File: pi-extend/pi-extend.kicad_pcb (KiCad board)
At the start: 2 copper layers, 53.3 x 67.1 mm, 5 parts, among them J1 Conn_02x20_Odd_Even, J2 Conn_01x20_Male, J3 Conn_01x20_Male, J4 Conn_01x02_Male, J5 Conn_01x02_Male

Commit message: pi extender 레이아웃 축소
Signed-off-by: Ju, Gyeong-min <jcmh74@gmail.com>
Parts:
- moved J4 21.4 mm to (138.7, 111.8)
- moved J5 21.4 mm to (186.9, 111.8)
- moved J2 12.2 mm to (148.8, 78.8)
- moved J3 12.2 mm to (176.8, 78.8)
- moved J1 12.1 mm to (138.7, 67.6)
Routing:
- net Net-(J1-Pad2): track 102.9 -> 86.5 mm
- net Net-(J1-Pad1): track 73.1 -> 57.1 mm
- net Net-(J1-Pad5): track 73.5 -> 57.5 mm
- net Net-(J1-Pad10): track 93.7 -> 78.0 mm
- net Net-(J1-Pad29): track 76.8 -> 76.0 mm
- net Net-(J1-Pad7): track 32.0 -> 31.2 mm
- net Net-(J1-Pad40): track 68.0 -> 67.2 mm
- net Net-(J1-Pad3): track 26.6 -> 25.8 mm
- net Net-(J1-Pad38): track 66.1 -> 65.4 mm
- net Net-(J1-Pad34): track 62.4 -> 61.6 mm
- net Net-(J1-Pad36): track 64.3 -> 63.5 mm
- net Net-(J1-Pad18): track 55.5 -> 56.1 mm
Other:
- board size 53.3 x 67.1 mm -> 53.4 x 65.9 mm
- board text added: "3V3 G2(SDA1) G3(SCL1) G4 GND G17 G27 G22 3V3 G10(MOSI) G9(MISO) G11(SCLK) GND ID_SD G5 G6 G13 G19 G26 GND"
- board text added: "5V 5V GND G14(TXD0) G15(RXD0) G18 GND G23 G24 GND G25 G8(CE0) G7(CE1) ID_SC GND G12 GND G16 G20 G21"
- board text removed: "3V3 SDA1 SCL1 GP4 GND GP17 GP27 GP22 3V3 MOSI MISO SCLK GND EED GP5 GP6 GP13 GP19 GP26 GND"
- board text removed: "5V 5V GND TXD0 RXD0 GP18 GND GP23 GP24 GND GP25 CE0 CE1 EEC GND GP12 GND GP16 GP20 GP21"

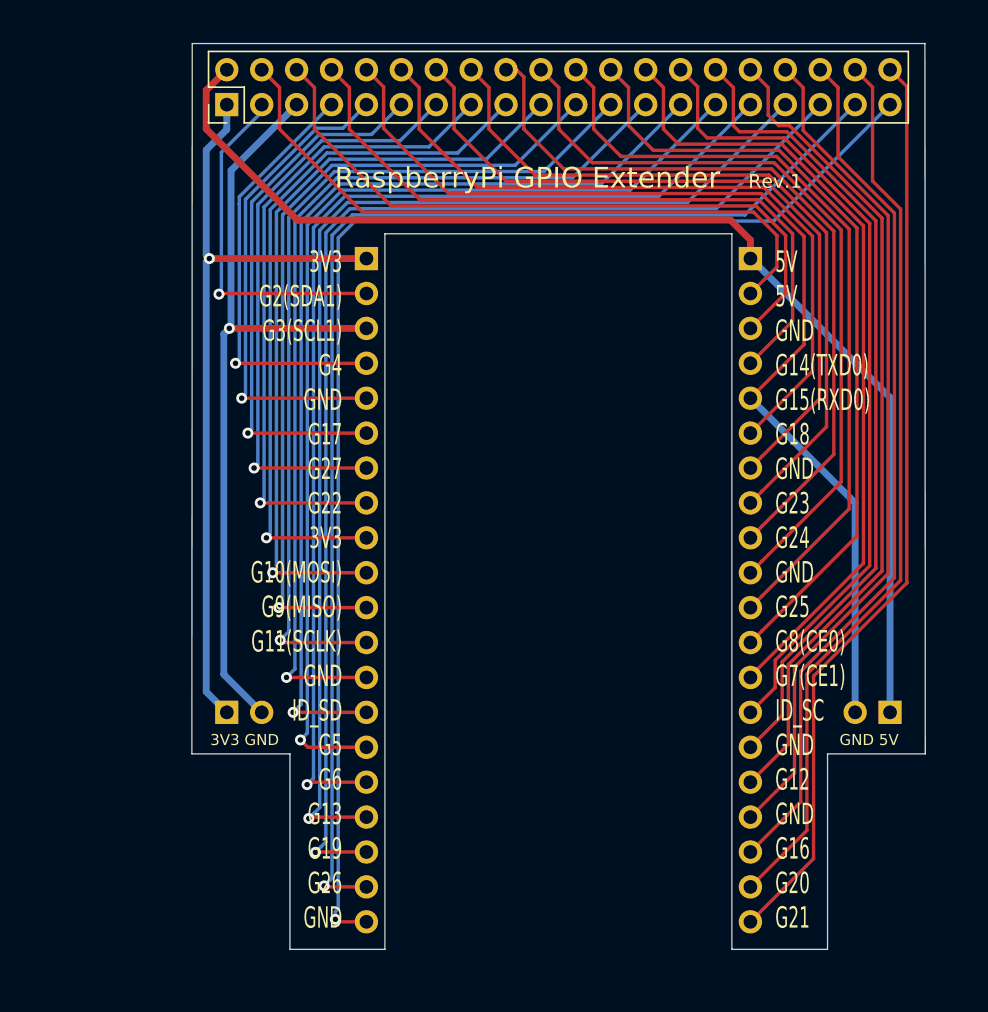
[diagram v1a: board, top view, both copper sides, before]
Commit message: pi-extender 레이아웃 변경
Signed-off-by: Ju, Gyeong-min <jcmh74@gmail.com>
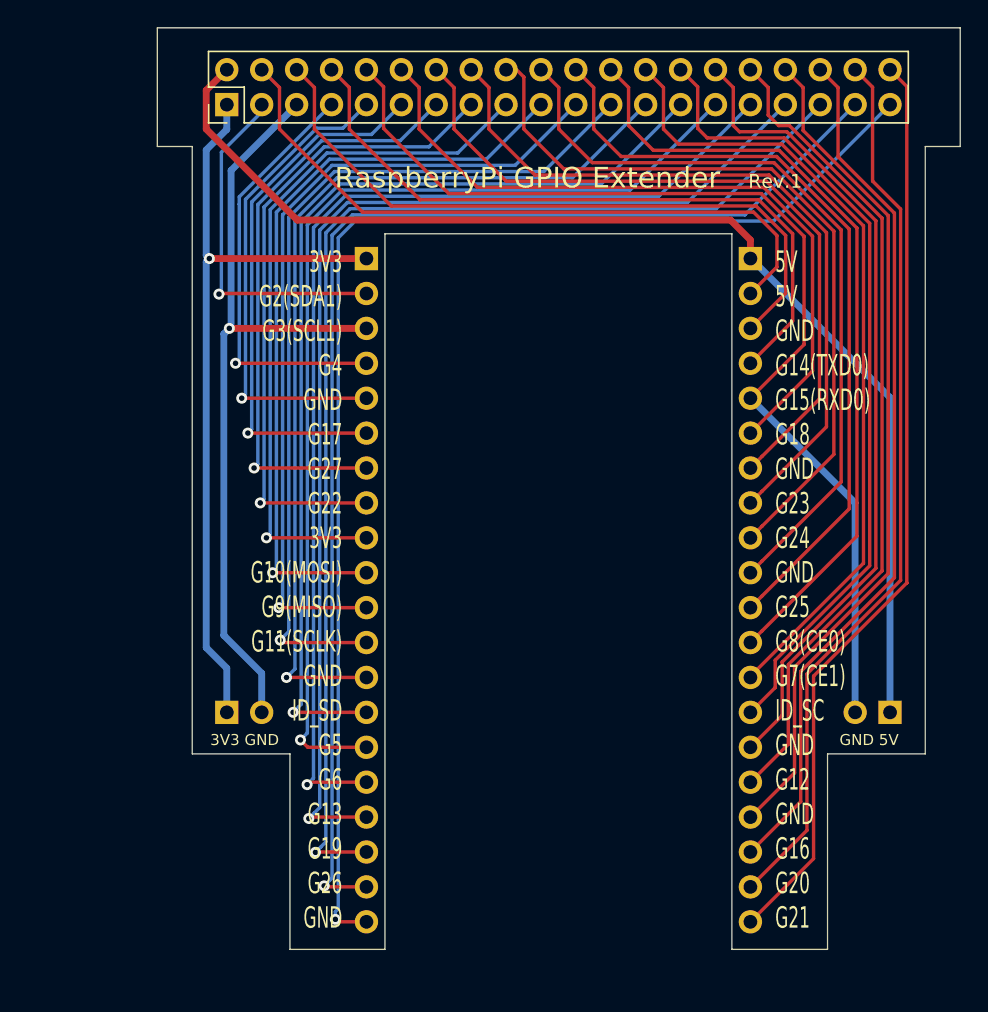
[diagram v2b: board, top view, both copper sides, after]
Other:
- board size 53.4 x 65.9 mm -> 58.4 x 67.1 mm
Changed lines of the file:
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@@
   (general
     (thickness 1.6)
-    (drawings 18)
-    (tracks 318)
+    (drawings 22)
+    (tracks 320)
     (zones 0)
     (modules 5)
@@
     )
   )
+  (gr_line (start 189.484 70.612) (end 189.484 114.808) (layer Edge.Cuts) (width 0.05))
+  (gr_line (start 189.484 70.612) (end 192.024 70.612) (layer Edge.Cuts) (width 0.05))
+  (gr_line (start 136.144 70.612) (end 136.144 114.808) (layer Edge.Cuts) (width 0.05))
+  (gr_line (start 136.144 70.612) (end 133.604 70.612) (layer Edge.Cuts) (width 0.05))
   (gr_line (start 143.256 114.808) (end 143.256 129.032) (layer Edge.Cuts) (width 0.05))
-  (gr_line (start 143.256 114.808) (end 136.1186 114.808) (layer Edge.Cuts) (width 0.05))
+  (gr_line (start 143.256 114.808) (end 136.144 114.808) (layer Edge.Cuts) (width 0.05))
   (gr_line (start 182.372 114.808) (end 182.372 129.032) (layer Edge.Cuts) (width 0.05))
   (gr_line (start 189.484 114.808) (end 182.372 114.808) (layer Edge.Cuts) (width 0.05))
@@
   (gr_line (start 150.1648 129.032) (end 150.1648 76.962) (layer Edge.Cuts) (width 0.05))
   (gr_line (start 143.256 129.032) (end 150.1648 129.032) (layer Edge.Cuts) (width 0.05))
-  (gr_line (start 136.144 63.119) (end 136.1186 114.808) (layer Edge.Cuts) (width 0.05))
-  (gr_line (start 189.4586 63.119) (end 136.144 63.119) (layer Edge.Cuts) (width 0.05))
-  (gr_line (start 189.484 114.808) (end 189.4586 63.119) (layer Edge.Cuts) (width 0.05))
+  (gr_line (start 133.604 61.976) (end 133.604 70.612) (layer Edge.Cuts) (width 0.05))
+  (gr_line (start 192.024 61.976) (end 133.604 61.976) (layer Edge.Cuts) (width 0.05))
+  (gr_line (start 192.024 70.612) (end 192.024 61.976) (layer Edge.Cuts) (width 0.05))
   (gr_line (start 175.4124 129.032) (end 182.372 129.032) (layer Edge.Cuts) (width 0.05))
   (gr_line (start 175.4124 76.962) (end 175.4124 129.032) (layer Edge.Cuts) (width 0.05))
@@
   (segment (start 138.6586 67.564) (end 138.6586 69.3674) (width 0.5) (layer B.Cu) (net 1))
   (segment (start 137.16 78.994) (end 137.3886 78.7654) (width 0.5) (layer B.Cu) (net 1))
-  (segment (start 137.16 110.2868) (end 137.16 78.994) (width 0.5) (layer B.Cu) (net 1))
-  (segment (start 138.6586 111.7854) (end 137.16 110.2868) (width 0.5) (layer B.Cu) (net 1))
+  (segment (start 137.16 107.0737) (end 137.16 78.994) (width 0.5) (layer B.Cu) (net 1))
+  (segment (start 138.6586 108.5723) (end 137.16 107.0737) (width 0.5) (layer B.Cu) (net 1))
+  (segment (start 138.6586 111.7854) (end 138.6586 108.5723) (width 0.5) (layer B.Cu) (net 1))
   (segment (start 176.7586 77.4154) (end 176.7586 78.7654) (width 0.5) (layer F.Cu) (net 2))
   (segment (start 137.16 66.5226) (end 137.16 69.342) (width 0.5) (layer F.Cu) (net 2))
@@
   (segment (start 143.7386 67.564) (end 143.7386 67.5894) (width 0.5) (layer B.Cu) (net 5))
   (segment (start 138.443413 84.245397) (end 138.843412 83.845398) (width 0.5) (layer B.Cu) (net 5))
-  (segment (start 138.443413 109.030213) (end 138.443413 84.245397) (width 0.5) (layer B.Cu) (net 5))
-  (segment (start 141.1986 111.7854) (end 138.443413 109.030213) (width 0.5) (layer B.Cu) (net 5))
+  (segment (start 138.443413 106.185413) (end 138.443413 84.245397) (width 0.5) (layer B.Cu) (net 5))
+  (segment (start 141.1986 108.9406) (end 138.443413 106.185413) (width 0.5) (layer B.Cu) (net 5))
+  (segment (start 141.1986 111.7854) (end 141.1986 108.9406) (width 0.5) (layer B.Cu) (net 5))
   (segment (start 179.324 81.28) (end 179.324 77.087589) (width 0.25) (layer F.Cu) (net 6))
   (segment (start 176.7586 83.8454) (end 179.324 81.28) (width 0.25) (layer F.Cu) (net 6))

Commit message: pi-extender gnd 핀 위치 변경
Signed-off-by: Ju, Gyeong-min <jcmh74@gmail.com>
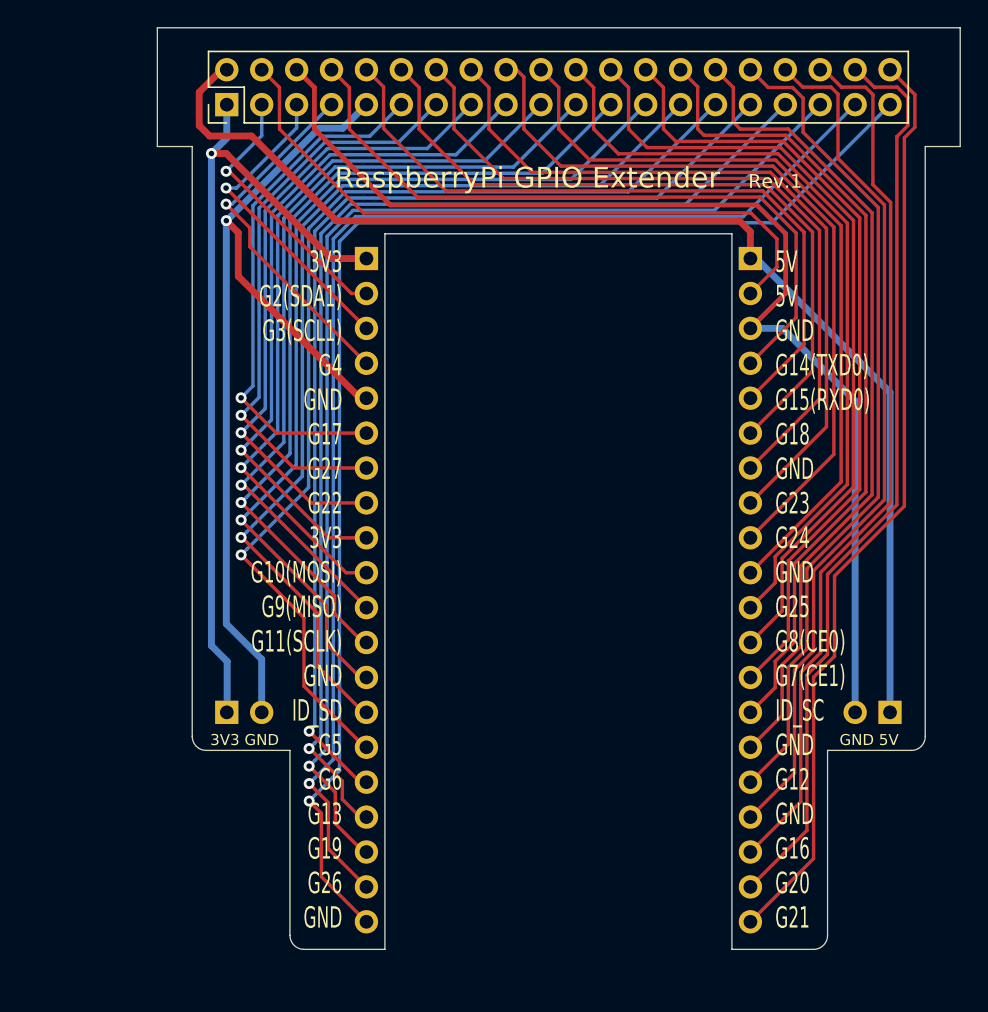
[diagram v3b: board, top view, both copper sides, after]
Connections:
- J4 pad 2: Net-(J1-Pad5) -> Net-(J1-Pad9)
- J5 pad 2: Net-(J1-Pad10) -> Net-(J1-Pad6)
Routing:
- net Net-(J1-Pad5): track 57.5 -> 23.1 mm
- net Net-(J1-Pad9): track 35.3 -> 67.9 mm
- net Net-(J1-Pad6): track 50.2 -> 82.7 mm
- net Net-(J1-Pad10): track 78.0 -> 52.2 mm
- net Net-(J1-Pad3): track 25.8 -> 19.8 mm
- net Net-(J1-Pad7): track 31.2 -> 26.5 mm
- net Net-(J1-Pad31): track 80.6 -> 77.8 mm
- net Net-(J1-Pad33): track 85.0 -> 82.5 mm
- net Net-(J1-Pad1): track 57.1 -> 59.6 mm
- net Net-(J1-Pad35): track 89.0 -> 87.0 mm
- net Net-(J1-Pad21): track 59.7 -> 58.2 mm
- net Net-(J1-Pad38): track 65.4 -> 66.9 mm
- net Net-(J1-Pad19): track 55.7 -> 54.2 mm
- net Net-(J1-Pad2): track 86.5 -> 87.9 mm
- net Net-(J1-Pad17): track 51.6 -> 50.3 mm
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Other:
- outline, holes or cut-outs redrawn

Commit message: pi-extend 폰트 크기 줄임
Signed-off-by: Ju, Gyeong-min <jcmh74@gmail.com>
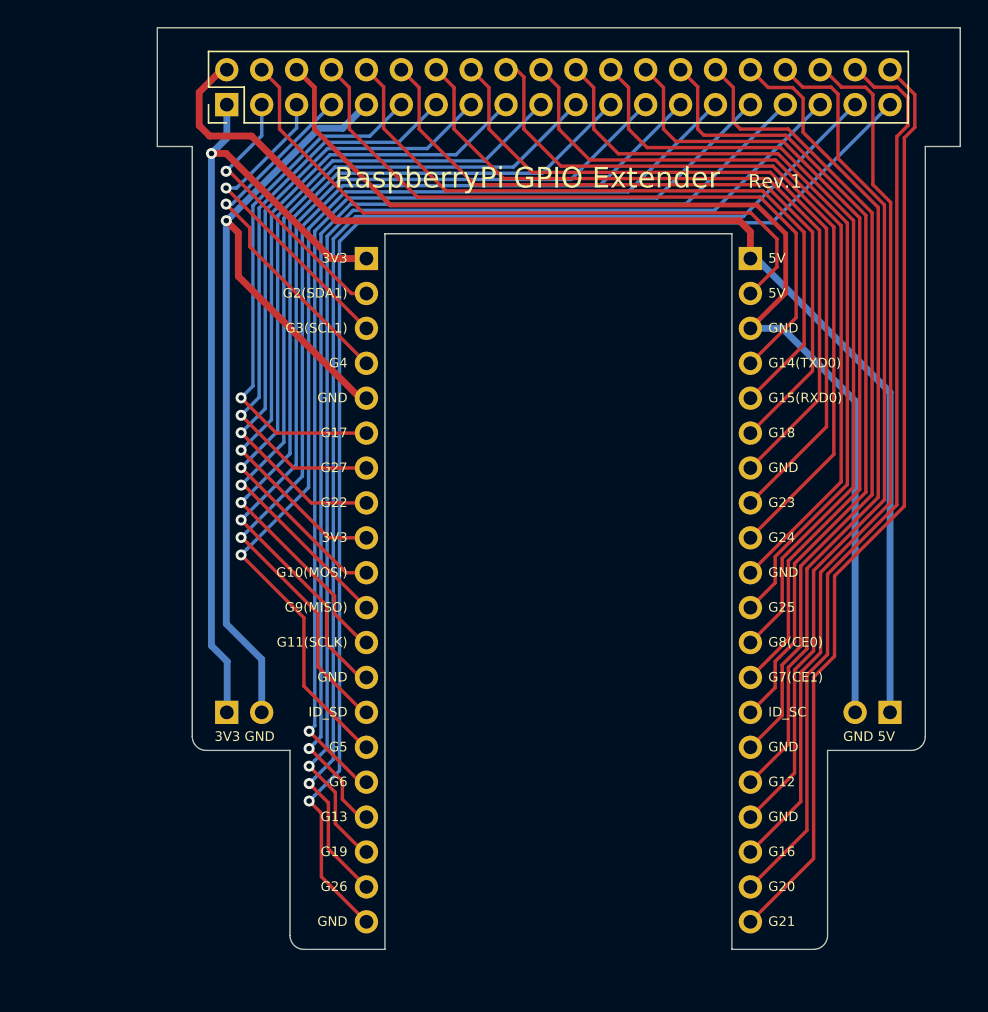
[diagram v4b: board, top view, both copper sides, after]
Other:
- board text added: "3V3"
- board text added: "5V"
- board text added: "G10(MOSI)"
- board text added: "G11(SCLK)"
- board text added: "G12"
- board text added: "G13"
- board text added: "G14(TXD0)"
- board text added: "G15(RXD0)"
- board text added: "G16"
- board text added: "G17"
- board text added: "G18"
- board text added: "G19"
- board text added: "G2(SDA1)"
- board text added: "G20"
- board text added: "G21"
- board text added: "G22"
- board text added: "G23"
- board text added: "G24"
- board text added: "G25"
- board text added: "G26"
- board text added: "G27"
- board text added: "G3(SCL1)"
- board text added: "G4"
- board text added: "G5"
- board text added: "G6"
- board text added: "G7(CE1)"
- board text added: "G8(CE0)"
- board text added: "G9(MISO)"
- board text added: "GND"
- board text added: "ID_SC"
- board text added: "ID_SD"
- board text removed: "3V3 G2(SDA1) G3(SCL1) G4 GND G17 G27 G22 3V3 G10(MOSI) G9(MISO) G11(SCLK) GND ID_SD G5 G6 G13 G19 G26 GND"
- board text removed: "5V 5V GND G14(TXD0) G15(RXD0) G18 GND G23 G24 GND G25 G8(CE0) G7(CE1) ID_SC GND G12 GND G16 G20 G21"

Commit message: pi-extend 전원핀 위치 선택 가능하도록 확장
Signed-off-by: Ju, Gyeong-min <jcmh74@gmail.com>
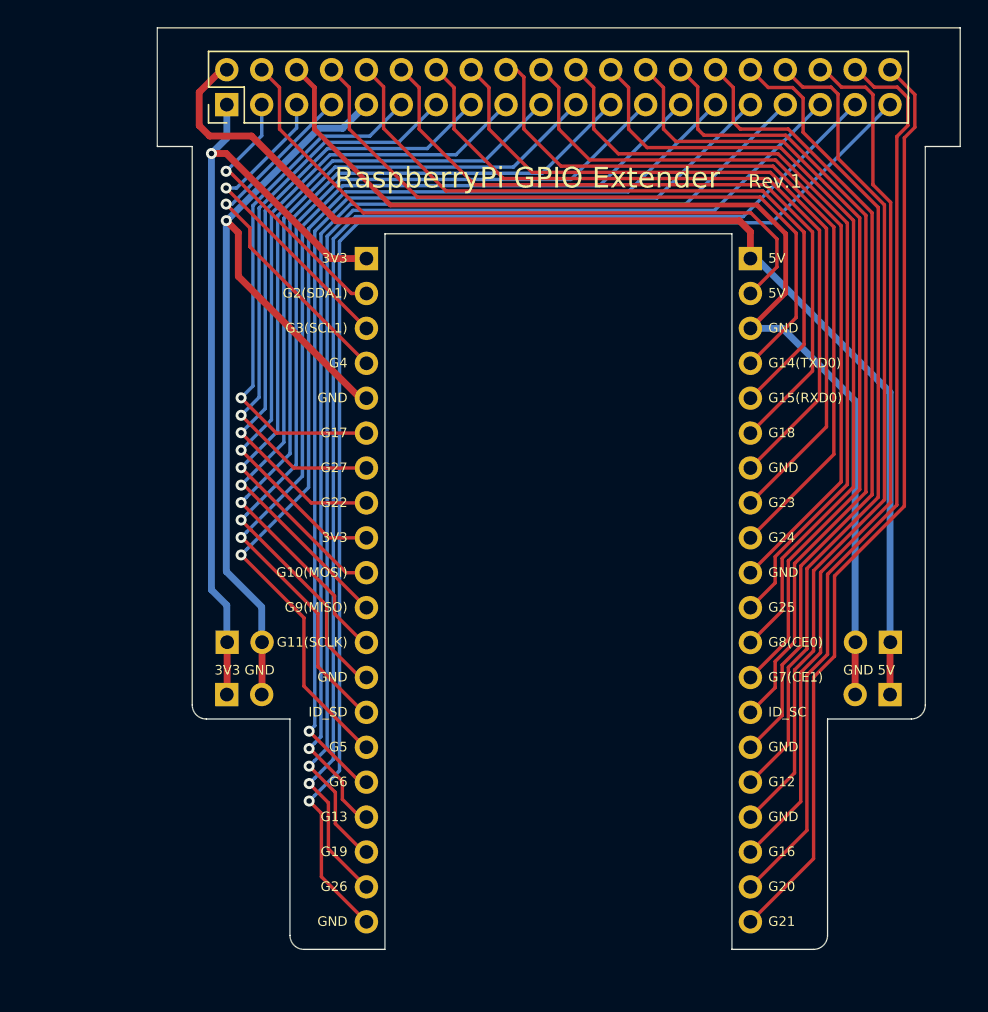
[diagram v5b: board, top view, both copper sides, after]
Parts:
- added J6: Conn_01x02_Male, Connector_PinHeader_2.54mm:PinHeader_1x02_P2.54mm_Vertical, B.Cu at (138.7, 106.7)
- added J7: Conn_01x02_Male, Connector_PinHeader_2.54mm:PinHeader_1x02_P2.54mm_Vertical, B.Cu at (186.9, 106.7)
- moved J4 1.30 mm to (138.7, 110.5)
- moved J5 1.30 mm to (186.9, 110.5)
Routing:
- net Net-(J1-Pad1): track 59.6 -> 58.3 mm
- net Net-(J1-Pad2): track 87.9 -> 86.6 mm
- net Net-(J1-Pad9): track 67.9 -> 66.7 mm
- net Net-(J1-Pad6): track 82.7 -> 81.4 mm
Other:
- outline, holes or cut-outs redrawn

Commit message: pi-extend 실크 마크 보강
Signed-off-by: Ju, Gyeong-min <jcmh74@gmail.com>
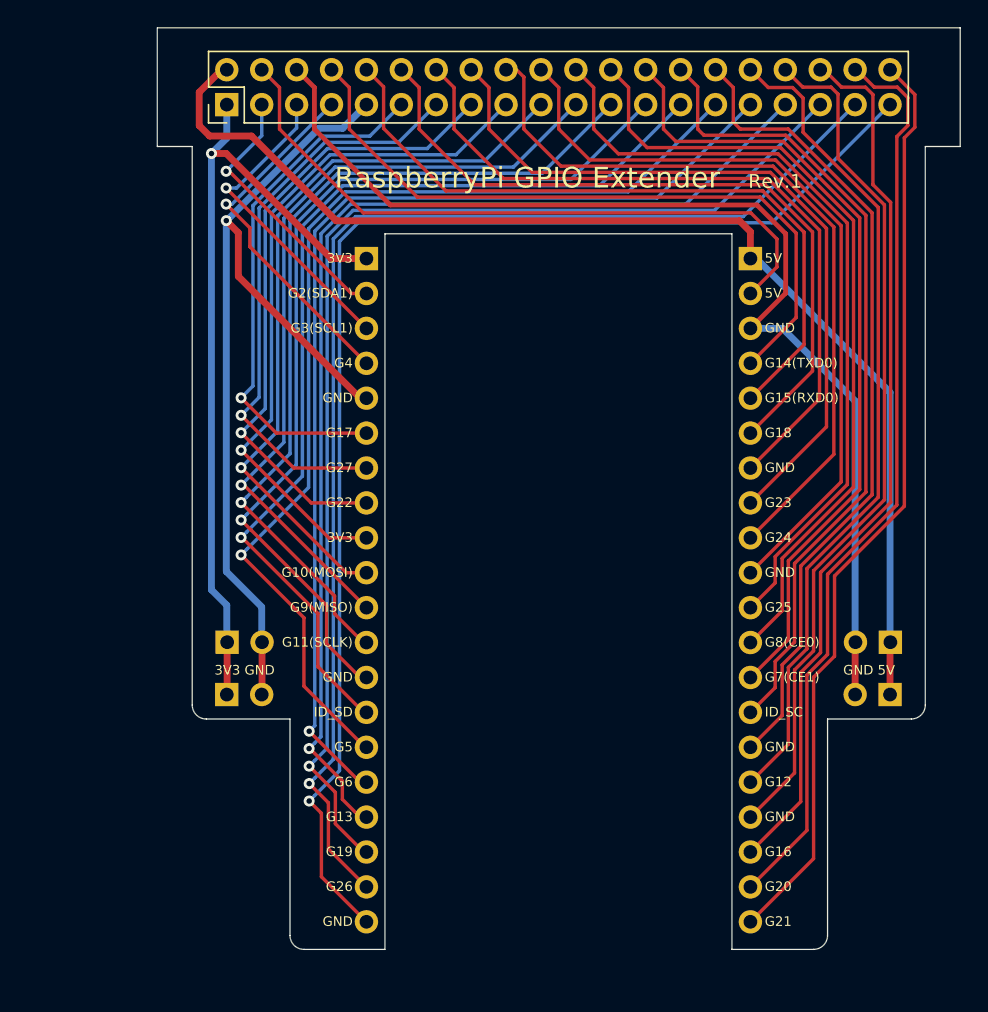
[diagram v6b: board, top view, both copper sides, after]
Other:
- board text added: "Select suitable pin for Breadboard"
